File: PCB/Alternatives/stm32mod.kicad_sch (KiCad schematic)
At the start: 32 parts, among them X1 Crystal

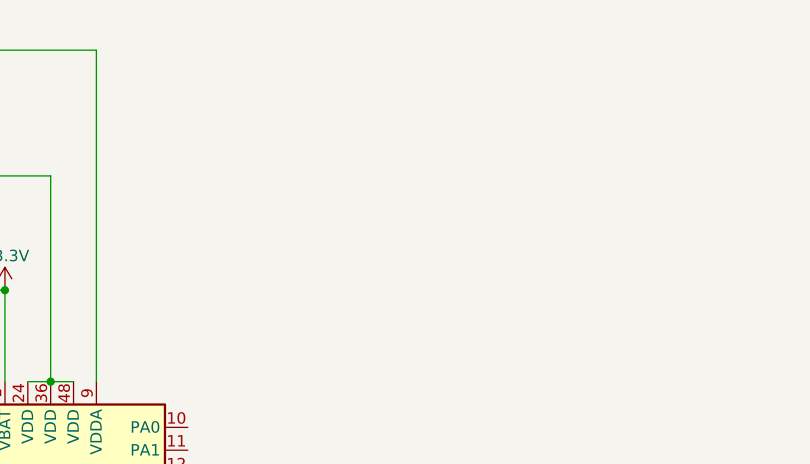
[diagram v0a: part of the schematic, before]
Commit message: Removed stm32, we're using a BluePill instead.
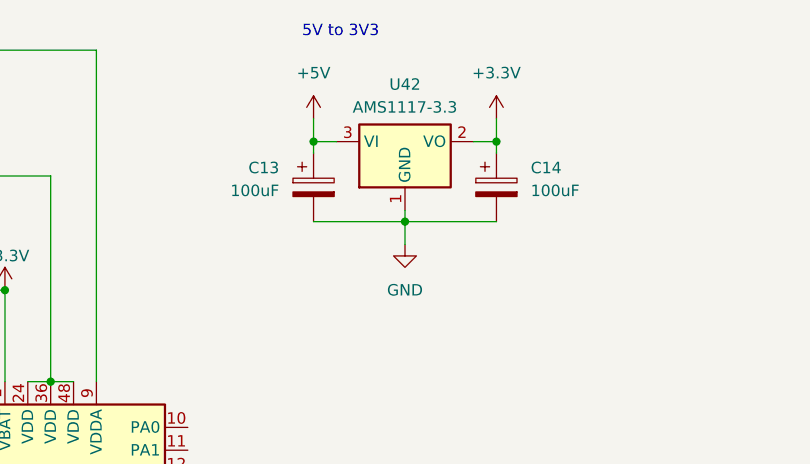
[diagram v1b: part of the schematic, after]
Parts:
- added C13, C14: 100uF, Capacitor_Tantalum_SMD:CP_EIA-3528-15_AVX-H, symbol Device:C_Polarized
- added U42: AMS1117-3.3, Package_TO_SOT_SMD:SOT-223-3_TabPin2, symbol Regulator_Linear:AMS1117-3.3
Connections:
- net +3.3V: now also C14.1, U42.2 (VO)
- net +5V: now also C13.1, U42.3 (VI)
- net GND: now also C13.2, C14.2, U42.1 (GND)
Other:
- note added: "5V to 3V3"
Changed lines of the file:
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@@
   (junction (at 59.69 25.4) (diameter 0) (color 0 0 0 0)
   )
+  (junction (at 125.73 27.94) (diameter 0) (color 0 0 0 0)
+  )
   (junction (at 40.64 39.37) (diameter 0) (color 0 0 0 0)
   )
@@
   (junction (at 27.94 31.75) (diameter 0) (color 0 0 0 0)
   )
+  (junction (at 115.57 36.83) (diameter 0) (color 0 0 0 0)
+  )
   (junction (at 46.99 31.75) (diameter 0) (color 0 0 0 0)
   )
@@
   (junction (at 53.34 31.75) (diameter 0) (color 0 0 0 0)
   )
+  (junction (at 105.41 27.94) (diameter 0) (color 0 0 0 0)
+  )
   (junction (at 59.69 39.37) (diameter 0) (color 0 0 0 0)
   )
@@
     (stroke (width 0) (type default))
   )
+  (wire (pts (xy 115.57 35.56) (xy 115.57 36.83))
+    (stroke (width 0) (type default))
+  )
   (wire (pts (xy 59.69 25.4) (xy 64.77 25.4))
     (stroke (width 0) (type default))
@@
     (stroke (width 0) (type default))
   )
+  (wire (pts (xy 107.95 27.94) (xy 105.41 27.94))
+    (stroke (width 0) (type default))
+  )
   (wire (pts (xy 121.92 168.91) (xy 121.92 171.45))
     (stroke (width 0) (type default))
@@
     (stroke (width 0) (type default))
   )
+  (wire (pts (xy 115.57 39.37) (xy 115.57 36.83))
+    (stroke (width 0) (type default))
+  )
   (wire (pts (xy 81.28 179.07) (xy 86.36 179.07))
     (stroke (width 0) (type default))
@@
     (stroke (width 0) (type default))
   )
+  (wire (pts (xy 123.19 27.94) (xy 125.73 27.94))
+    (stroke (width 0) (type default))
+  )
   (wire (pts (xy 24.13 31.75) (xy 27.94 31.75))
     (stroke (width 0) (type default))
   )
+  (wire (pts (xy 115.57 36.83) (xy 125.73 36.83))
+    (stroke (width 0) (type default))
+  )
   (wire (pts (xy 46.99 72.39) (xy 46.99 77.47))
     (stroke (width 0) (type default))
@@
     (stroke (width 0) (type default))
   )
+  (wire (pts (xy 105.41 27.94) (xy 105.41 29.21))
+    (stroke (width 0) (type default))
+  )
   (wire (pts (xy 81.28 17.78) (xy 81.28 54.61))
     (stroke (width 0) (type default))
   )
+  (wire (pts (xy 105.41 36.83) (xy 115.57 36.83))
+    (stroke (width 0) (type default))
+  )
   (wire (pts (xy 111.76 179.07) (xy 111.76 182.88))
     (stroke (width 0) (type default))
@@
     (stroke (width 0) (type default))
   )
+  (wire (pts (xy 105.41 27.94) (xy 105.41 25.4))
+    (stroke (width 0) (type default))
+  )
+  (wire (pts (xy 125.73 25.4) (xy 125.73 27.94))
+    (stroke (width 0) (type default))
+  )
   (wire (pts (xy 44.45 163.83) (xy 54.61 163.83))
     (stroke (width 0) (type default))
@@
   )
   (wire (pts (xy 68.58 179.07) (xy 68.58 182.88))
+    (stroke (width 0) (type default))
+  )
+  (wire (pts (xy 125.73 29.21) (xy 125.73 27.94))
     (stroke (width 0) (type default))
   )
@@
     (effects (font (size 1.27 1.27)) (justify left bottom))
   )
+  (text "5V to 3V3" (at 104.14 16.51 0)
+    (effects (font (size 1.27 1.27)) (justify left bottom))
+  )
   (text "Indicator LEDs" (at 104.14 149.86 0)
     (effects (font (size 1.27 1.27)) (justify left bottom))
@@
         (path "/d2f5552d-48c0-49b0-8e54-6764f47ed1da/5a7a16c1-b018-4a19-b382-77ab07b68c52/2030ad47-566c-4a6b-b217-7789d857619d"
           (reference "X1") (unit 1)
+        )
+      )
+    )
+  )
+  (symbol (lib_id "power:+5V") (at 105.41 25.4 0) (unit 1)
+    (in_bom yes) (on_board yes) (dnp no) (fields_autoplaced)
+    (property "Reference" "#PWR0214" (at 105.41 29.21 0)
+      (effects (font (size 1.27 1.27)) hide)
+    )
+    (property "Value" "+5V" (at 105.41 20.32 0)
+      (effects (font (size 1.27 1.27)))
+    )
+    (property "Footprint" "" (at 105.41 25.4 0)
+      (effects (font (size 1.27 1.27)) hide)
+    )
+    (property "Datasheet" "" (at 105.41 25.4 0)
+      (effects (font (size 1.27 1.27)) hide)
+    )
+    (pin "1")
+    (instances
+      (project "PCB"
+        (path "/d2f5552d-48c0-49b0-8e54-6764f47ed1da/5a7a16c1-b018-4a19-b382-77ab07b68c52/2030ad47-566c-4a6b-b217-7789d857619d"
+          (reference "#PWR0214") (unit 1)
         )
       )
@@
     )
   )
+  (symbol (lib_id "Device:C_Polarized") (at 125.73 33.02 0) (unit 1)
+    (in_bom yes) (on_board yes) (dnp no) (fields_autoplaced)
+    (property "Reference" "C14" (at 129.54 30.861 0)
+      (effects (font (size 1.27 1.27)) (justify left))
+    )
+    (property "Value" "100uF" (at 129.54 33.401 0)
+      (effects (font (size 1.27 1.27)) (justify left))
+    )
+    (property "Footprint" "Capacitor_Tantalum_SMD:CP_EIA-3528-15_AVX-H" (at 126.6952 36.83 0)
+      (effects (font (size 1.27 1.27)) hide)
+    )
+    (property "Datasheet" "https://jlcpcb.com/partdetail/KyoceraAvx-TAJB107K006RNJ/C16133" (at 125.73 33.02 0)
+      (effects (font (size 1.27 1.27)) hide)
+    )
+    (property "LCSC" "C16133" (at 125.73 33.02 0)
+      (effects (font (size 1.27 1.27)) hide)
+    )
+    (pin "1")
+    (pin "2")
+    (instances
+      (project "PCB"
+        (path "/d2f5552d-48c0-49b0-8e54-6764f47ed1da/5a7a16c1-b018-4a19-b382-77ab07b68c52/2030ad47-566c-4a6b-b217-7789d857619d"
+          (reference "C14") (unit 1)
+        )
+      )
+    )
+  )
   (symbol (lib_id "power:GND") (at 165.1 182.88 0) (unit 1)
     (in_bom yes) (on_board yes) (dnp no) (fields_autoplaced)
@@
         (path "/d2f5552d-48c0-49b0-8e54-6764f47ed1da/5a7a16c1-b018-4a19-b382-77ab07b68c52/2030ad47-566c-4a6b-b217-7789d857619d"
           (reference "#PWR0211") (unit 1)
+        )
+      )
+    )
+  )
+  (symbol (lib_id "power:+3.3V") (at 125.73 25.4 0) (unit 1)
+    (in_bom yes) (on_board yes) (dnp no) (fields_autoplaced)
+    (property "Reference" "#PWR0216" (at 125.73 29.21 0)
+      (effects (font (size 1.27 1.27)) hide)
+    )
+    (property "Value" "+3.3V" (at 125.73 20.32 0)
+      (effects (font (size 1.27 1.27)))
+    )
+    (property "Footprint" "" (at 125.73 25.4 0)
+      (effects (font (size 1.27 1.27)) hide)
+    )
+    (property "Datasheet" "" (at 125.73 25.4 0)
+      (effects (font (size 1.27 1.27)) hide)
+    )
+    (pin "1")
+    (instances
+      (project "PCB"
+        (path "/d2f5552d-48c0-49b0-8e54-6764f47ed1da/5a7a16c1-b018-4a19-b382-77ab07b68c52/2030ad47-566c-4a6b-b217-7789d857619d"
+          (reference "#PWR0216") (unit 1)
         )
       )
@@
     )
   )
+  (symbol (lib_id "power:GND") (at 115.57 39.37 0) (unit 1)
+    (in_bom yes) (on_board yes) (dnp no) (fields_autoplaced)
+    (property "Reference" "#PWR0215" (at 115.57 45.72 0)
+      (effects (font (size 1.27 1.27)) hide)
+    )
+    (property "Value" "GND" (at 115.57 44.45 0)
+      (effects (font (size 1.27 1.27)))
+    )
+    (property "Footprint" "" (at 115.57 39.37 0)
+      (effects (font (size 1.27 1.27)) hide)
+    )
+    (property "Datasheet" "" (at 115.57 39.37 0)
+      (effects (font (size 1.27 1.27)) hide)
+    )
+    (pin "1")
+    (instances
+      (project "PCB"
+        (path "/d2f5552d-48c0-49b0-8e54-6764f47ed1da/5a7a16c1-b018-4a19-b382-77ab07b68c52/2030ad47-566c-4a6b-b217-7789d857619d"
+          (reference "#PWR0215") (unit 1)
+        )
+      )
+    )
+  )
+  (symbol (lib_id "Device:C_Polarized") (at 105.41 33.02 0) (unit 1)
+    (in_bom yes) (on_board yes) (dnp no) (fields_autoplaced)
+    (property "Reference" "C13" (at 101.6 30.861 0)
+      (effects (font (size 1.27 1.27)) (justify right))
+    )
+    (property "Value" "100uF" (at 101.6 33.401 0)
+      (effects (font (size 1.27 1.27)) (justify right))
+    )
+    (property "Footprint" "Capacitor_Tantalum_SMD:CP_EIA-3528-15_AVX-H" (at 106.3752 36.83 0)
+      (effects (font (size 1.27 1.27)) hide)
+    )
+    (property "Datasheet" "https://jlcpcb.com/partdetail/KyoceraAvx-TAJB107K006RNJ/C16133" (at 105.41 33.02 0)
+      (effects (font (size 1.27 1.27)) hide)
+    )
+    (property "LCSC" "C16133" (at 105.41 33.02 0)
+      (effects (font (size 1.27 1.27)) hide)
+    )
+    (pin "1")
+    (pin "2")
+    (instances
+      (project "PCB"
+        (path "/d2f5552d-48c0-49b0-8e54-6764f47ed1da/5a7a16c1-b018-4a19-b382-77ab07b68c52/2030ad47-566c-4a6b-b217-7789d857619d"
+          (reference "C13") (unit 1)
+        )
+      )
+    )
+  )
   (symbol (lib_id "Device:LED") (at 133.35 175.26 90) (unit 1)
     (in_bom yes) (on_board yes) (dnp no) (fields_autoplaced)
@@
         )
       )
+    )
+  )
+  (symbol (lib_id "Regulator_Linear:AMS1117-3.3") (at 115.57 27.94 0) (unit 1)
+    (in_bom yes) (on_board yes) (dnp no) (fields_autoplaced)
+    (property "Reference" "U42" (at 115.57 21.59 0)
+      (effects (font (size 1.27 1.27)))
+    )
+    (property "Value" "AMS1117-3.3" (at 115.57 24.13 0)
+      (effects (font (size 1.27 1.27)))
+    )
+    (property "Footprint" "Package_TO_SOT_SMD:SOT-223-3_TabPin2" (at 115.57 22.86 0)
+      (effects (font (size 1.27 1.27)) hide)
+    )
+    (property "Datasheet" "http://www.advanced-monolithic.com/pdf/ds1117.pdf" (at 118.11 34.29 0)
+      (effects (font (size 1.27 1.27)) hide)
+    )
+    (pin "1")
+    (pin "2")
+    (pin "3")
+    (instances
+      (project "PCB"
+        (path "/d2f5552d-48c0-49b0-8e54-6764f47ed1da/5a7a16c1-b018-4a19-b382-77ab07b68c52/2030ad47-566c-4a6b-b217-7789d857619d"
+          (reference "U42") (unit 1)
+        )
+      )
